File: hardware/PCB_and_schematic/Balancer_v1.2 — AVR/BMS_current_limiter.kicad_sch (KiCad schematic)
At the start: 40 parts, among them J1 BATT_OUT, J12 External Current Shunt, J13 BATT_IN, Q1 BC817, Q2 BC337, Q3 BC327, Q4 PMOS, Q5 PMOS, Q6 BC337, Q7 BC327, Q8 BC817

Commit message: Update electrical schematic and BMS schematic
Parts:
- removed D2, D7: LL4148, Diode_SMD:D_MiniMELF, symbol Diode:LL4148
- added R36, R37: 10k, Resistor_SMD:R_0805_2012Metric, symbol Device:R
- added U2: 74AHCT125, Package_SO:SOIC-14_3.9x8.7mm_P1.27mm, symbol 74xx:74AHCT125
- R6: value 1k -> 10R
- R7: value 100R -> 10R
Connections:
- net PWM_OUT_CHRG: now also R36.1, U2.12; no longer D8.1 (K), R11.1
- net PWM_OUT_DISCH: now also R37.1, U2.9; no longer D1.1 (K), R1.1
- new net: D1.1 (K), R1.1, U2.8
- new net: D8.1 (K), R11.1, U2.11
- new net +5V: R36.2, R37.2
- new net GND: U2.10, U2.13

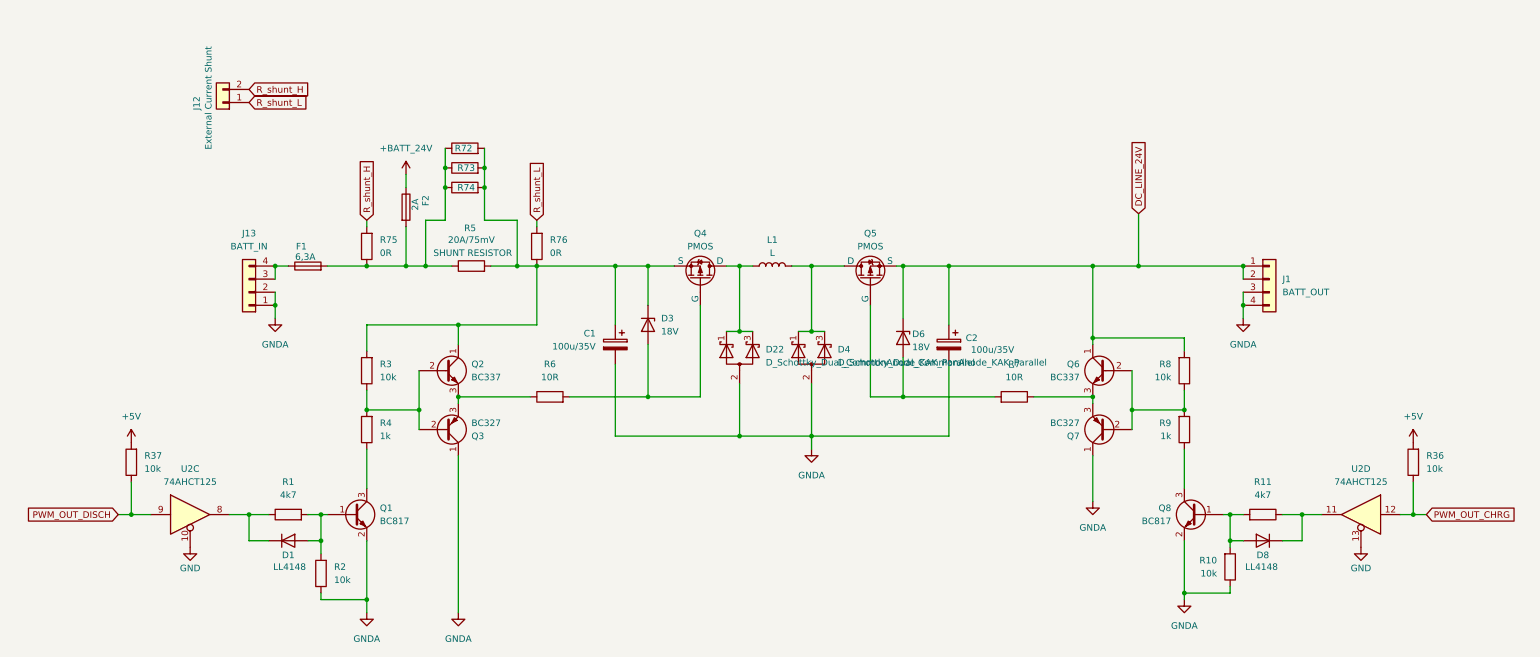
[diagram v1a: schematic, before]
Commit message: Update balacer schematic - change fan drive circuit,  fix current limiter drive
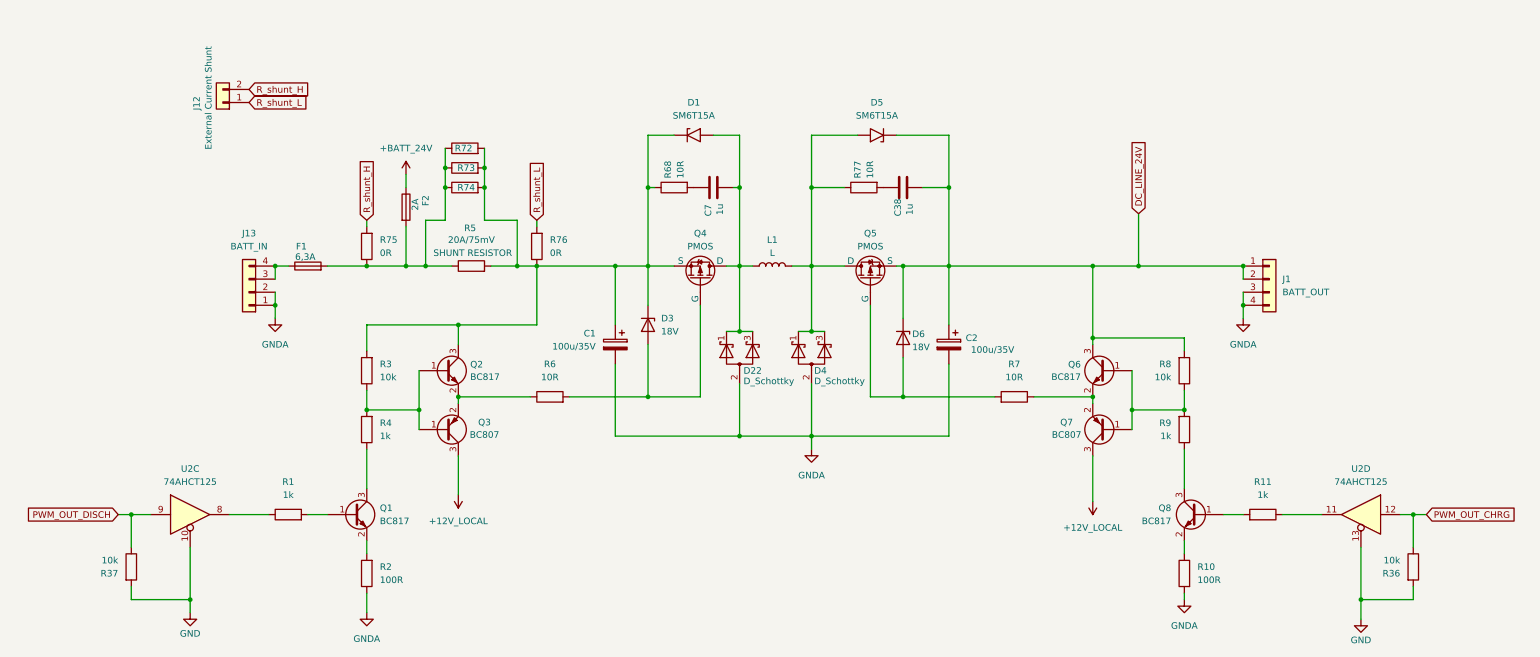
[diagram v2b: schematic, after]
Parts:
- removed D1, D8: LL4148, Diode_SMD:D_MiniMELF, symbol Diode:LL4148
- removed Q2, Q6: BC337, My-Footprints:TO-92_Inline_Wide, symbol Transistor_BJT:BC337
- removed Q3, Q7: BC327, My-Footprints:TO-92_Inline_Wide, symbol Transistor_BJT:BC327
- added C38, C7: 1u, Capacitor_THT:C_Disc_D5.0mm_W2.5mm_P2.50mm, symbol Device:C
- added D1, D5: SM6T15A, Diode_SMD:D_SMB, symbol Diode:SM6T15A
- added Q2, Q6: BC817, Package_TO_SOT_SMD:SOT-23, symbol Transistor_BJT:BC817
- added Q3, Q7: BC807, Package_TO_SOT_SMD:SOT-23, symbol Transistor_BJT:BC807
- added R68, R77: 10R, Resistor_THT:R_Axial_DIN0204_L3.6mm_D1.6mm_P7.62mm_Horizontal, symbol Device:R
- D22, D4: value D_Schottky_Dual_CommonAnode_KAK_Parallel -> D_Schottky
- R1, R11: value 4k7 -> 1k
- R10, R2: value 10k -> 100R
- R3, R8: footprint Resistor_SMD:R_0805_2012Metric -> Resistor_SMD:R_1206_3216Metric
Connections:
- net +5V is gone; now on net GND: R36.2, R37.2
- net DC_LINE_24V: now also C38.2, D5.1 (A1), Q6.3 (C)
- net GNDA: now also R10.2; no longer Q1.2 (E), Q8.2 (E), R10.1
- net at Q1.1 (B), R1.2: no longer R2.2
- net at D22.1 (K), D22.3 (K), L1.1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: now also C7.2, D1.2 (A2)
- net at D4.1 (K), D4.3 (K), L1.2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: now also D5.2 (A2), R77.1
- net at R8.1, R9.2: now also Q6.1 (B), Q7.1 (B)
- net at R7.1: now also Q6.2 (E), Q7.2 (E)
- net at C1.1, D3.1 (K), Q4.3 (S)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: now also D1.1 (A1), Q2.3 (C), R68.1
- net at R3.1, R4.2: now also Q2.1 (B), Q3.1 (B)
- net at Q8.1 (B), R11.2: no longer R10.2
- net at R6.1: now also Q2.2 (E), Q3.2 (E)
- new net: C38.1, R77.2
- new net: Q8.2 (E), R10.1
- new net: C7.1, R68.2
- new net: Q1.2 (E), R2.2
- new net +12V_LOCAL: Q3.3 (C), Q7.3 (C)
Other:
- moved on the sheet: R36, R37

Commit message: balacer routing update
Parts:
- removed D3, D6: 18V, Diode_SMD:D_MiniMELF, symbol Device:D_Zener
- removed Q4, Q5: PMOS, My-Footprints:TO-220-3_V_Thick_Pads, symbol Simulation_SPICE:PMOS
- added D11, D3: SM6T15A, Diode_SMD:D_SMB, symbol Diode:SM6T15A
- added Q4, Q5: IRF4905, Package_TO_SOT_THT:TO-220-3_Vertical, symbol Transistor_FET:IRF4905
- L1: footprint Inductor_THT:L_Axial_L26.0mm_D11.0mm_P30.48mm_Horizontal_Fastron_77A -> My-Footprints:Inductor_Toroidal
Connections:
- net DC_LINE_24V: now also D3.1 (A1), Q5.3 (S)
- net at C7.2, D1.2 (A2), D22.1 (K)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: now also Q4.2 (D)
- net at D4.1 (K), D4.3 (K), D5.2 (A2)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: now also Q5.2 (D)
- net at R7.2: now also D3.2 (A2), Q5.1 (G)
- net at C1.1, D1.1 (A1), Q2.3 (C)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: now also D11.1 (A1), Q4.3 (S)
- net at R6.2: now also D11.2 (A2), Q4.1 (G)

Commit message: balancer pcb update
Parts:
- Q4, Q5: footprint Package_TO_SOT_THT:TO-220-3_Vertical -> My-Footprints:TO-220-3_V_Thick_Pads
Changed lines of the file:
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@@
 			)
 		)
-		(property "Footprint" "Package_TO_SOT_THT:TO-220-3_Vertical"
+		(property "Footprint" "My-Footprints:TO-220-3_V_Thick_Pads"
 			(at 140.335 54.61 0)
 			(effects
@@
 			)
 		)
-		(property "Footprint" "Package_TO_SOT_THT:TO-220-3_Vertical"
+		(property "Footprint" "My-Footprints:TO-220-3_V_Thick_Pads"
 			(at 177.165 54.61 0)
 			(effects

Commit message: balancer routing done
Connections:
- net GND: no longer R36.2, R37.2
- net PWM_OUT_CHRG: now also R36.2; no longer R36.1
- net PWM_OUT_DISCH: now also R37.2; no longer R37.1
- new net +5V: R36.1, R37.1
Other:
- moved on the sheet: R36, R37
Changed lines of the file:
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@@
 	)
 	(junction
+		(at 31.75 105.41)
+		(diameter 0)
+		(color 0 0 0 0)
+	)
+	(junction
 		(at 87.63 85.09)
 		(diameter 0)
@@
 	)
 	(junction
-		(at 270.51 121.92)
-		(diameter 0)
-		(color 0 0 0 0)
-	)
-	(junction
 		(at 236.22 85.09)
 		(diameter 0)
@@
 	)
 	(junction
-		(at 43.18 121.92)
-		(diameter 0)
-		(color 0 0 0 0)
-	)
-	(junction
 		(at 218.44 57.15)
 		(diameter 0)
@@
 	)
 	(junction
-		(at 31.75 105.41)
-		(diameter 0)
-		(color 0 0 0 0)
-	)
-	(junction
 		(at 125.73 57.15)
 		(diameter 0)
@@
 	(wire
 		(pts
-			(xy 31.75 121.92) (xy 31.75 119.38)
-		)
-		(stroke
-			(width 0)
-			(type default)
-		)
-	)
-	(wire
-		(pts
-			(xy 43.18 124.46) (xy 43.18 121.92)
-		)
-		(stroke
-			(width 0)
-			(type default)
-		)
-	)
-	(wire
-		(pts
-			(xy 270.51 121.92) (xy 280.67 121.92)
+			(xy 43.18 111.76) (xy 43.18 124.46)
 		)
 		(stroke
@@
 	(wire
 		(pts
-			(xy 280.67 105.41) (xy 278.13 105.41)
+			(xy 278.13 105.41) (xy 280.67 105.41)
 		)
 		(stroke
@@
 	(wire
 		(pts
+			(xy 280.67 105.41) (xy 283.21 105.41)
+		)
+		(stroke
+			(width 0)
+			(type default)
+		)
+	)
+	(wire
+		(pts
 			(xy 163.83 69.85) (xy 166.37 69.85)
 		)
@@
 	(wire
 		(pts
-			(xy 270.51 125.73) (xy 270.51 121.92)
+			(xy 270.51 111.76) (xy 270.51 125.73)
 		)
 		(stroke
@@
 	(wire
 		(pts
-			(xy 280.67 119.38) (xy 280.67 121.92)
-		)
-		(stroke
-			(width 0)
-			(type default)
-		)
-	)
-	(wire
-		(pts
 			(xy 132.08 82.55) (xy 142.24 82.55)
 		)
@@
 	(wire
 		(pts
-			(xy 280.67 111.76) (xy 280.67 105.41)
+			(xy 31.75 100.33) (xy 31.75 105.41)
 		)
 		(stroke
@@
 	(wire
 		(pts
-			(xy 270.51 121.92) (xy 270.51 111.76)
-		)
-		(stroke
-			(width 0)
-			(type default)
-		)
-	)
-	(wire
-		(pts
 			(xy 88.9 57.15) (xy 88.9 48.26)
 		)
@@
 	(wire
 		(pts
-			(xy 43.18 121.92) (xy 31.75 121.92)
-		)
-		(stroke
-			(width 0)
-			(type default)
-		)
-	)
-	(wire
-		(pts
 			(xy 77.47 81.28) (xy 77.47 85.09)
 		)
@@
 	(wire
 		(pts
-			(xy 31.75 111.76) (xy 31.75 105.41)
-		)
-		(stroke
-			(width 0)
-			(type default)
-		)
-	)
-	(wire
-		(pts
 			(xy 95.25 82.55) (xy 109.22 82.55)
 		)
@@
 	(wire
 		(pts
-			(xy 31.75 105.41) (xy 35.56 105.41)
-		)
-		(stroke
-			(width 0)
-			(type default)
-		)
-	)
-	(wire
-		(pts
 			(xy 110.49 57.15) (xy 106.68 57.15)
 		)
@@
 	(wire
 		(pts
-			(xy 77.47 48.26) (xy 77.47 49.53)
+			(xy 280.67 102.87) (xy 280.67 105.41)
 		)
 		(stroke
@@
 	(wire
 		(pts
-			(xy 132.08 41.91) (xy 132.08 57.15)
+			(xy 77.47 48.26) (xy 77.47 49.53)
 		)
 		(stroke
@@
 	(wire
 		(pts
-			(xy 283.21 105.41) (xy 280.67 105.41)
+			(xy 132.08 41.91) (xy 132.08 57.15)
 		)
 		(stroke
@@
 	(wire
 		(pts
-			(xy 218.44 71.12) (xy 218.44 72.39)
+			(xy 31.75 105.41) (xy 35.56 105.41)
 		)
 		(stroke
@@
 	(wire
 		(pts
-			(xy 43.18 121.92) (xy 43.18 111.76)
+			(xy 218.44 71.12) (xy 218.44 72.39)
 		)
 		(stroke
@@
 	(symbol
 		(lib_id "Device:R")
-		(at 31.75 115.57 0)
+		(at 31.75 96.52 0)
 		(unit 1)
 		(exclude_from_sim no)
@@
 		(dnp no)
 		(property "Reference" "R37"
-			(at 29.21 116.8401 0)
+			(at 29.21 97.7901 0)
 			(effects
 				(font
@@
 		)
 		(property "Value" "10k"
-			(at 29.21 114.3001 0)
+			(at 29.21 95.2501 0)
 			(effects
 				(font
@@
 		)
 		(property "Footprint" "Resistor_SMD:R_0805_2012Metric"
-			(at 29.972 115.57 90)
+			(at 29.972 96.52 90)
 			(effects
 				(font
@@
 		)
 		(property "Datasheet" "~"
-			(at 31.75 115.57 0)
+			(at 31.75 96.52 0)
 			(effects
 				(font
@@
 		)
 		(property "Description" "Resistor"
-			(at 31.75 115.57 0)
+			(at 31.75 96.52 0)
 			(effects
 				(font
@@
 	(symbol
 		(lib_id "Device:R")
-		(at 280.67 115.57 0)
+		(at 280.67 99.06 0)
 		(unit 1)
 		(exclude_from_sim no)
@@
 		(dnp no)
 		(property "Reference" "R36"
-			(at 278.13 116.8401 0)
+			(at 278.13 100.3301 0)
 			(effects
 				(font
@@
 		)
 		(property "Value" "10k"
-			(at 278.13 114.3001 0)
+			(at 278.13 97.7901 0)
 			(effects
 				(font
@@
 		)
 		(property "Footprint" "Resistor_SMD:R_0805_2012Metric"
-			(at 278.892 115.57 90)
+			(at 278.892 99.06 90)
 			(effects
 				(font
@@
 		)
 		(property "Datasheet" "~"
-			(at 280.67 115.57 0)
+			(at 280.67 99.06 0)
 			(effects
 				(font
@@
 		)
 		(property "Description" "Resistor"
-			(at 280.67 115.57 0)
+			(at 280.67 99.06 0)
 			(effects
 				(font
@@
 	)
 	(symbol
+		(lib_id "power:+5V")
+		(at 280.67 95.25 0)
+		(unit 1)
+		(exclude_from_sim no)
+		(in_bom yes)
+		(on_board yes)
+		(dnp no)
+		(fields_autoplaced yes)
+		(property "Reference" "#PWR041"
+			(at 280.67 99.06 0)
+			(effects
+				(font
+					(size 1.27 1.27)
+				)
+				(hide yes)
+			)
+		)
+		(property "Value" "+5V"
+			(at 280.67 90.17 0)
+			(effects
+				(font
+					(size 1.27 1.27)
+				)
+			)
+		)
+		(property "Footprint" ""
+			(at 280.67 95.25 0)
+			(effects
+				(font
+					(size 1.27 1.27)
+				)
+				(hide yes)
+			)
+		)
+		(property "Datasheet" ""
+			(at 280.67 95.25 0)
+			(effects
+				(font
+					(size 1.27 1.27)
+				)
+				(hide yes)
+			)
+		)
+		(property "Description" "Power symbol creates a global label with name \"+5V\""
+			(at 280.67 95.25 0)
+			(effects
+				(font
+					(size 1.27 1.27)
+				)
+				(hide yes)
+			)
+		)
+		(pin "1"
+		)
+		(instances
+			(project "Balancer"
+				(path "/555ba40f-9abb-4b99-82c6-07e888fda9fd/f65ef685-3e95-4f8a-97fe-0688761539e6"
+					(reference "#PWR041")
+					(unit 1)
+				)
+			)
+		)
+	)
+	(symbol
 		(lib_id "Connector_Generic:Conn_01x04")
 		(at 252.73 59.69 0)
@@
 					(unit 1)
 				)
+			)
+		)
+	)
+	(symbol
+		(lib_id "power:+5V")
+		(at 31.75 92.71 0)
+		(unit 1)
+		(exclude_from_sim no)
+		(in_bom yes)
+		(on_board yes)
+		(dnp no)
+		(fields_autoplaced yes)
+		(property "Reference" "#PWR047"
+			(at 31.75 96.52 0)
+			(effects
+				(font
+					(size 1.27 1.27)
+				)
+				(hide yes)
+			)
+		)
+		(property "Value" "+5V"
+			(at 31.75 87.63 0)
+			(effects
+				(font
+					(size 1.27 1.27)
+				)
+			)
+		)
+		(property "Footprint" ""
+			(at 31.75 92.71 0)
+			(effects
+				(font
+					(size 1.27 1.27)
+				)
+				(hide yes)
+			)
+		)
+		(property "Datasheet" ""
+			(at 31.75 92.71 0)
+			(effects
+				(font
+					(size 1.27 1.27)
+				)
+				(hide yes)
+			)
+		)
+		(property "Description" "Power symbol creates a global label with name \"+5V\""
+			(at 31.75 92.71 0)
+			(effects
+				(font
+					(size 1.27 1.27)
+				)
+				(hide yes)
+			)
+		)
+		(pin "1"
+		)
+		(instances
+			(project "Balancer"
+				(path "/555ba40f-9abb-4b99-82c6-07e888fda9fd/f65ef685-3e95-4f8a-97fe-0688761539e6"
+					(reference "#PWR047")
+					(unit 1)
+				)

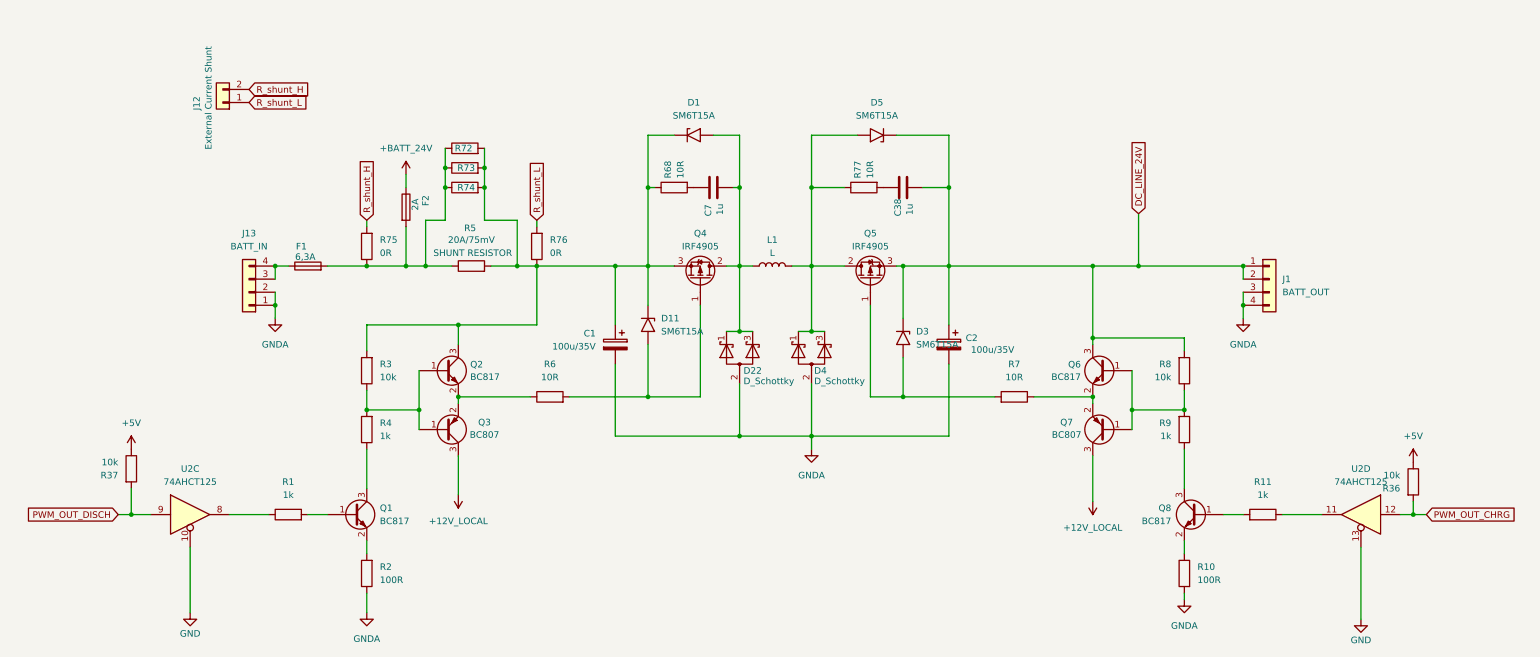
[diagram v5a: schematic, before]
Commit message: balancer pcb change smps diode footprint, schematic cleanup, designators arrangement, add mouting holes
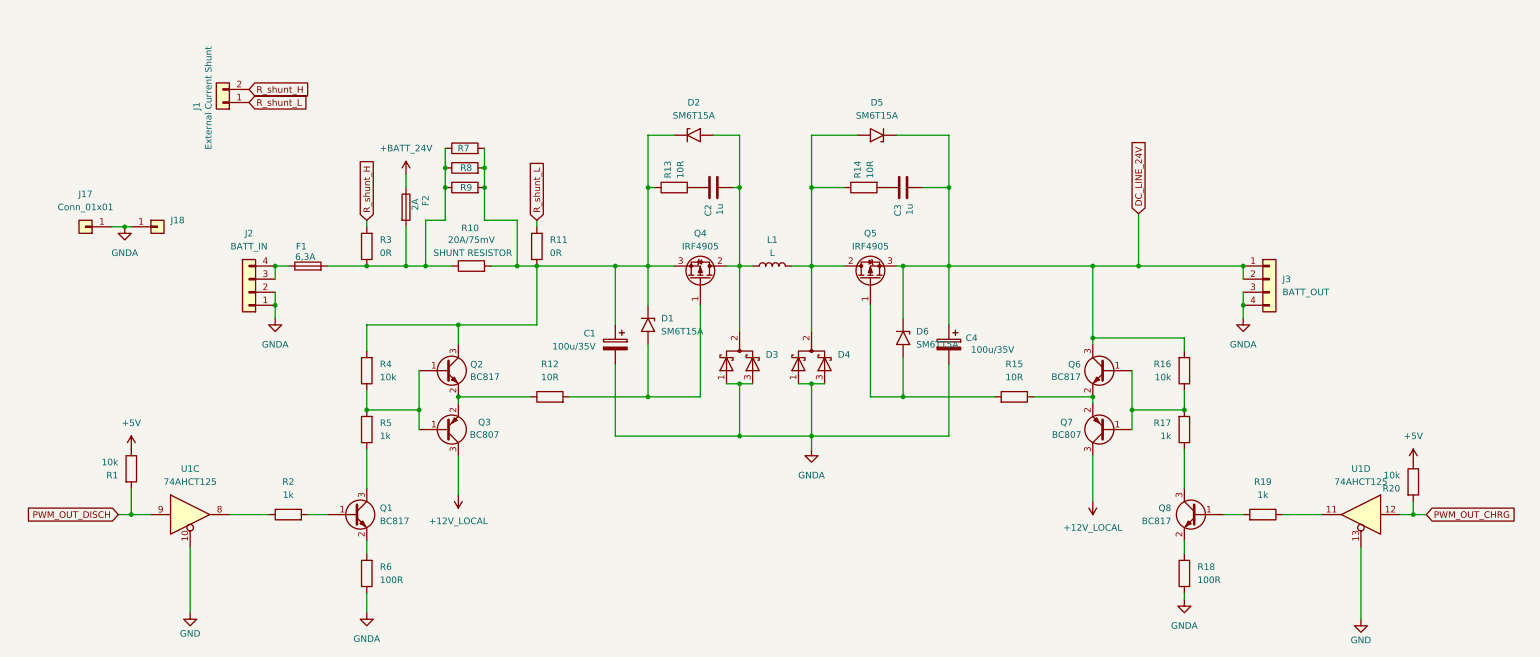
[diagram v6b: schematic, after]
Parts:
- removed D22, D4: D_Schottky, My-Footprints:TO-220-3_V_Thick_Pads, symbol Device:D_Schottky_Dual_CommonAnode_KAK_Parallel
- added D3, D4: ~, My-Footprints:TO-220-3_V_Thick_Pads, symbol Device:D_Schottky_Dual_CommonCathode_AKA_Parallel
- added J17: Conn_01x01, Connector_Wire:SolderWire-1.5sqmm_1x01_D1.7mm_OD3.9mm, symbol Connector_Generic:Conn_01x01
- added J18: ~, Connector_Wire:SolderWire-1.5sqmm_1x01_D1.7mm_OD3.9mm, symbol Connector_Generic:Conn_01x01
- renumbered C7 to C2, C38 to C3, C2 to C4, D11 to D1, D1 to D2, D3 to D6, J12 to J1, J13 to J2, J1 to J3, R37 to R1, R5 to R10, R76 to R11, R6 to R12, R68 to R13, R77 to R14, R7 to R15, R8 to R16, R9 to R17, R10 to R18, R11 to R19, R1 to R2, R36 to R20, R75 to R3, R3 to R4, R4 to R5, R2 to R6, R72 to R7, R73 to R8, R74 to R9, U2 to U1
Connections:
- net GNDA: now also D3.1 (K), D3.3 (K), D4.1 (K), D4.3 (K), J17.1 (Pin_1), J18.1 (Pin_1)
- net at C2.2, D2.2 (A2), L1.1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: now also D3.2 (A)
- net at D5.2 (A2), L1.2, Q5.2 (D)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: now also D4.2 (A)

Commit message: esp32 modbus easun working
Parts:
- D3, D4: value ~ -> YM3045
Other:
- moved on the sheet: C4
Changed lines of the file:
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@@
 	)
 	(junction
+		(at 194.31 57.15)
+		(diameter 0)
+		(color 0 0 0 0)
+	)
+	(junction
 		(at 92.71 38.1)
 		(diameter 0)
@@
 	(wire
 		(pts
-			(xy 190.5 57.15) (xy 218.44 57.15)
+			(xy 190.5 57.15) (xy 194.31 57.15)
 		)
 		(stroke
@@
 	(wire
 		(pts
+			(xy 194.31 57.15) (xy 218.44 57.15)
+		)
+		(stroke
+			(width 0)
+			(type default)
+		)
+	)
+	(wire
+		(pts
 			(xy 270.51 111.76) (xy 270.51 125.73)
 		)
@@
 	(wire
 		(pts
-			(xy 190.5 57.15) (xy 190.5 68.58)
+			(xy 194.31 57.15) (xy 194.31 68.58)
 		)
 		(stroke
@@
 	(wire
 		(pts
-			(xy 163.83 90.17) (xy 190.5 90.17)
+			(xy 163.83 90.17) (xy 194.31 90.17)
 		)
 		(stroke
@@
 	(wire
 		(pts
-			(xy 190.5 90.17) (xy 190.5 76.2)
+			(xy 194.31 90.17) (xy 194.31 76.2)
 		)
 		(stroke
@@
 		(on_board yes)
 		(dnp no)
-		(fields_autoplaced yes)
 		(property "Reference" "D3"
-			(at 154.94 74.3584 90)
+			(at 151.638 81.9149 90)
 			(effects
 				(font
@@
 			)
 		)
-		(property "Value" "~"
-			(at 154.94 76.2635 90)
+		(property "Value" "YM3045"
+			(at 151.638 83.82 90)
 			(effects
 				(font
@@
 	(symbol
 		(lib_id "Device:C_Polarized")
-		(at 190.5 72.39 0)
+		(at 194.31 72.39 0)
 		(mirror y)
 		(unit 1)
@@
 		(dnp no)
 		(property "Reference" "C4"
-			(at 196.088 71.12 0)
+			(at 199.898 71.12 0)
 			(effects
 				(font
@@
 		)
 		(property "Value" "100u/35V"
-			(at 203.2 73.406 0)
+			(at 207.01 73.406 0)
 			(effects
 				(font
@@
 		)
 		(property "Footprint" "Capacitor_THT:CP_Radial_D8.0mm_P3.50mm"
-			(at 189.5348 76.2 0)
+			(at 193.3448 76.2 0)
 			(effects
 				(font
@@
 		)
 		(property "Datasheet" "~"
-			(at 190.5 72.39 0)
+			(at 194.31 72.39 0)
 			(effects
 				(font
@@
 		)
 		(property "Description" "Polarized capacitor"
-			(at 190.5 72.39 0)
+			(at 194.31 72.39 0)
 			(effects
 				(font
@@
 		(on_board yes)
 		(dnp no)
-		(fields_autoplaced yes)
 		(property "Reference" "D4"
-			(at 168.91 74.3584 90)
+			(at 166.624 81.1529 90)
 			(effects
 				(font
@@
 			)
 		)
-		(property "Value" "~"
-			(at 168.91 76.2635 90)
+		(property "Value" "YM3045"
+			(at 166.624 83.058 90)
 			(effects
 				(font
@@
 		(on_board yes)
 		(dnp no)
-		(fields_autoplaced yes)
 		(property "Reference" "D6"
-			(at 184.15 69.8499 90)
+			(at 183.134 70.612 90)
 			(effects
 				(font
@@
 		)
 		(property "Value" "SM6T15A"
-			(at 184.15 72.3899 90)
+			(at 183.134 73.152 90)
 			(effects
 				(font
